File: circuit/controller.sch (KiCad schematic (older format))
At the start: 1 part, among them U7 ESP-12F

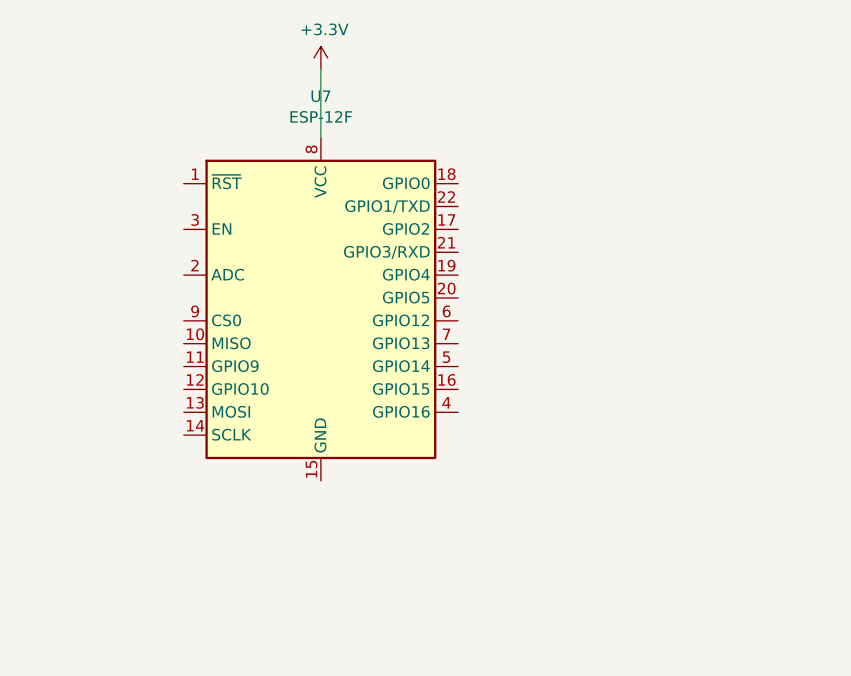
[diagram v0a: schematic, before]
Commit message: Added microcontroller circuit
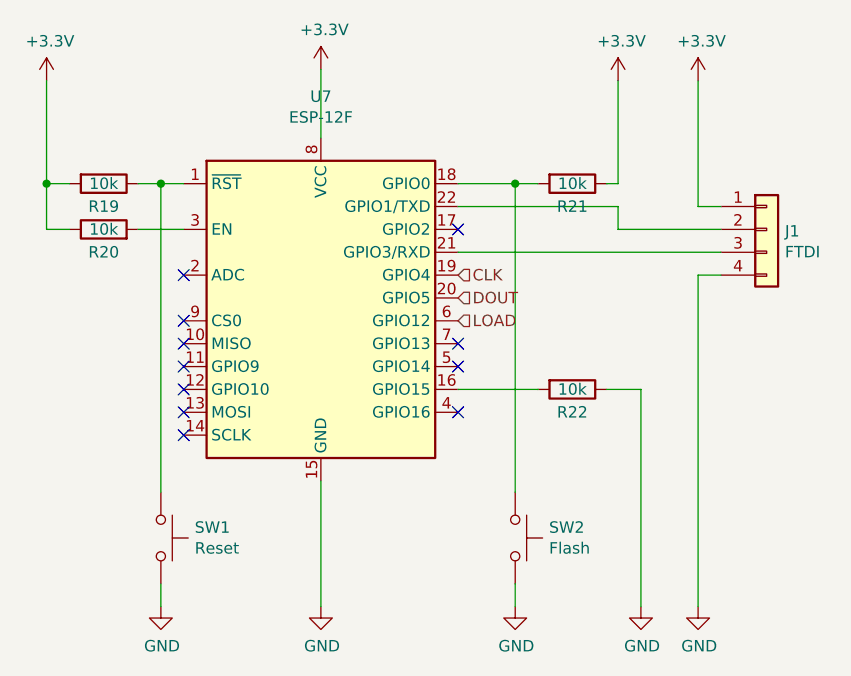
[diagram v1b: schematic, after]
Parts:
- added J1: FTDI, Connector_PinHeader_2.54mm:PinHeader_1x04_P2.54mm_Vertical, symbol Connector_Generic:Conn_01x04
- added R19, R20, R21, R22: 10k, Resistor_SMD:R_0805_2012Metric_Pad1.15x1.40mm_HandSolder, symbol Device:R
- added SW1: Reset, Button_Switch_SMD:SW_SPST_CK_RS282G05A3, symbol Switch:SW_Push
- added SW2: Flash, Button_Switch_SMD:SW_SPST_CK_RS282G05A3, symbol Switch:SW_Push
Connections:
- net +3V3: now also J1.1 (Pin_1), R19.2, R20.1, R21.1
- net at U7.1 (~RST): now also R19.1, SW1.1
- net GND: now reaches U7.15 (GND)
- net GND: now also J1.4 (Pin_4), R22.1, SW1.2, SW2.2
- net at U7.16 (GPIO15): now also R22.2
- net at U7.18 (GPIO0): now also R21.2, SW2.1
- net CLK: now reaches U7.19 (GPIO4)
- net DOUT: now reaches U7.20 (GPIO5)
- net at U7.21 (GPIO3/RXD): now also J1.3 (Pin_3)
- net at U7.22 (GPIO1/TXD): now also J1.2 (Pin_2)
- net at U7.3 (EN): now also R20.2
- net LOAD: now reaches U7.6 (GPIO12)
- no-connect marks 0 -> 11

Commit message: Changed to use hardware spi
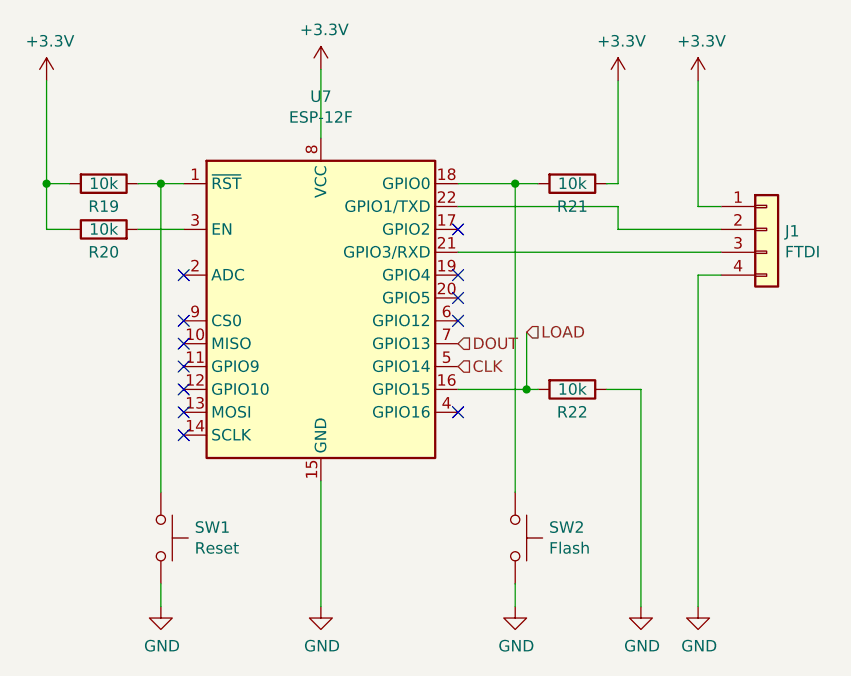
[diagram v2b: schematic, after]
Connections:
- net CLK: now also U7.5 (GPIO14); no longer U7.19 (GPIO4)
- net DOUT: now also U7.7 (GPIO13); no longer U7.20 (GPIO5)
- net LOAD: now also R22.2, U7.16 (GPIO15); no longer U7.6 (GPIO12)
- no-connect marks 11 -> 12
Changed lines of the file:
@@
 $EndComp
 Wire Wire Line
-	6000 4000 5650 4000
+	6000 4000 5950 4000
 $Comp
 L Device:R R21
@@
 Wire Wire Line
 	5050 4400 5050 4950
-Text HLabel 5650 3600 2    50   Input ~ 0
+Text HLabel 5650 3800 2    50   Input ~ 0
 DOUT
 NoConn ~ 5650 3300
-NoConn ~ 5650 3800
-NoConn ~ 5650 3900
 NoConn ~ 5650 4100
 NoConn ~ 4450 4200
@@
 NoConn ~ 4450 3700
 NoConn ~ 4450 3500
-Text HLabel 5650 3500 2    50   Input ~ 0
+Text HLabel 5650 3900 2    50   Input ~ 0
 CLK
-Text HLabel 5650 3700 2    50   Input ~ 0
+Text HLabel 5950 3750 2    50   Input ~ 0
 LOAD
+Wire Wire Line
+	5950 3750 5950 4000
+Connection ~ 5950 4000
+Wire Wire Line
+	5950 4000 5650 4000
+NoConn ~ 5650 3700
+NoConn ~ 5650 3600
+NoConn ~ 5650 3500
 $EndSCHEMATC
